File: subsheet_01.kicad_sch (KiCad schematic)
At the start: 0 parts

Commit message: schematic : place U1 and U2, the CPLD and the Gate array connector
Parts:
- added U1: ATF1508AS_L_100A_TQFP_JTAG_ENABLED_PHY, Package_QFP:TQFP-100_14x14mm_P0.5mm, symbol atf1508as-tqfp100-jtag:ATF1508AS_L_100A_TQFP_JTAG_ENABLED_PHY
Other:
- note added: "The north side of U1 is oriented toward the East side of U2, to hopefully have an easier routing of the 16 MHz clock."
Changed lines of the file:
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@@
     (comment 4 "Original repository : https://github.com/sporniket/...")
   )
+  (text "The north side of U1 is oriented toward the East side of U2,\nto hopefully have an easier routing of the 16 MHz clock."
+    (at 25.4 25.4 0)
+    (effects (font (size 2 2)) (justify left bottom))
+  )
+  (symbol (lib_id "atf1508as-tqfp100-jtag:ATF1508AS_L_100A_TQFP_JTAG_ENABLED_PHY") (at 106.68 130.81 270) (unit 1)
+    (in_bom yes) (on_board yes) (dnp no)
+    (property "Reference" "U1" (at 139.7 80.01 90)
+      (effects (font (size 1.27 1.27)) (justify left bottom))
+    )
+    (property "Value" "ATF1508AS_L_100A_TQFP_JTAG_ENABLED_PHY" (at 139.7 81.28 90)
+      (effects (font (size 1.27 1.27) bold) (justify left top))
+    )
+    (property "Footprint" "Package_QFP:TQFP-100_14x14mm_P0.5mm" (at 162.56 162.56 0)
+      (effects (font (size 1.27 1.27)) (justify left top) hide)
+    )
+    (property "Datasheet" "https://ww1.microchip.com/downloads/en/DeviceDoc/doc0784.pdf" (at 165.1 162.56 0)
+      (effects (font (size 1.27 1.27)) (justify left top) hide)
+    )
+    (pin "99")
+    (pin "45")
+    (pin "75")
+    (pin "74")
+    (pin "63")
+    (pin "81")
+    (pin "8")
+    (pin "35")
+    (pin "64")
+    (pin "72")
+    (pin "53")
+    (pin "38")
+    (pin "22")
+    (pin "69")
+    (pin "36")
+    (pin "71")
+    (pin "37")
+    (pin "88")
+    (pin "61")
+    (pin "82")
+    (pin "98")
+    (pin "96")
+    (pin "78")
+    (pin "34")
+    (pin "14")
+    (pin "1")
+    (pin "9")
+    (pin "49")
+    (pin "25")
+    (pin "84")
+    (pin "20")
+    (pin "41")
+    (pin "29")
+    (pin "4")
+    (pin "5")
+    (pin "42")
+    (pin "44")
+    (pin "46")
+    (pin "40")
+    (pin "43")
+    (pin "90")
+    (pin "28")
+    (pin "39")
+    (pin "2")
+    (pin "12")
+    (pin "13")
+    (pin "23")
+    (pin "24")
+    (pin "58")
+    (pin "11")
+    (pin "10")
+    (pin "100")
+    (pin "21")
+    (pin "68")
+    (pin "59")
+    (pin "52")
+    (pin "76")
+    (pin "15")
+    (pin "79")
+    (pin "86")
+    (pin "19")
+    (pin "66")
+    (pin "83")
+    (pin "7")
+    (pin "62")
+    (pin "89")
+    (pin "85")
+    (pin "16")
+    (pin "80")
+    (pin "51")
+    (pin "56")
+    (pin "94")
+    (pin "50")
+    (pin "77")
+    (pin "27")
+    (pin "26")
+    (pin "32")
+    (pin "93")
+    (pin "67")
+    (pin "54")
+    (pin "33")
+    (pin "97")
+    (pin "95")
+    (pin "30")
+    (pin "18")
+    (pin "3")
+    (pin "55")
+    (pin "91")
+    (pin "47")
+    (pin "70")
+    (pin "31")
+    (pin "87")
+    (pin "65")
+    (pin "6")
+    (pin "73")
+    (pin "17")
+    (pin "48")
+    (pin "57")
+    (pin "60")
+    (pin "92")
+    (instances
+      (project "mo5-ga-motorola-repl--atf1508"
+        (path "/04881907-557f-4bbf-81fb-63c3424a1f56/01c5ed34-7d13-4e1e-8741-0da82dc21da9"
+          (reference "U1") (unit 1)
+        )
+      )
+    )
+  )
 )

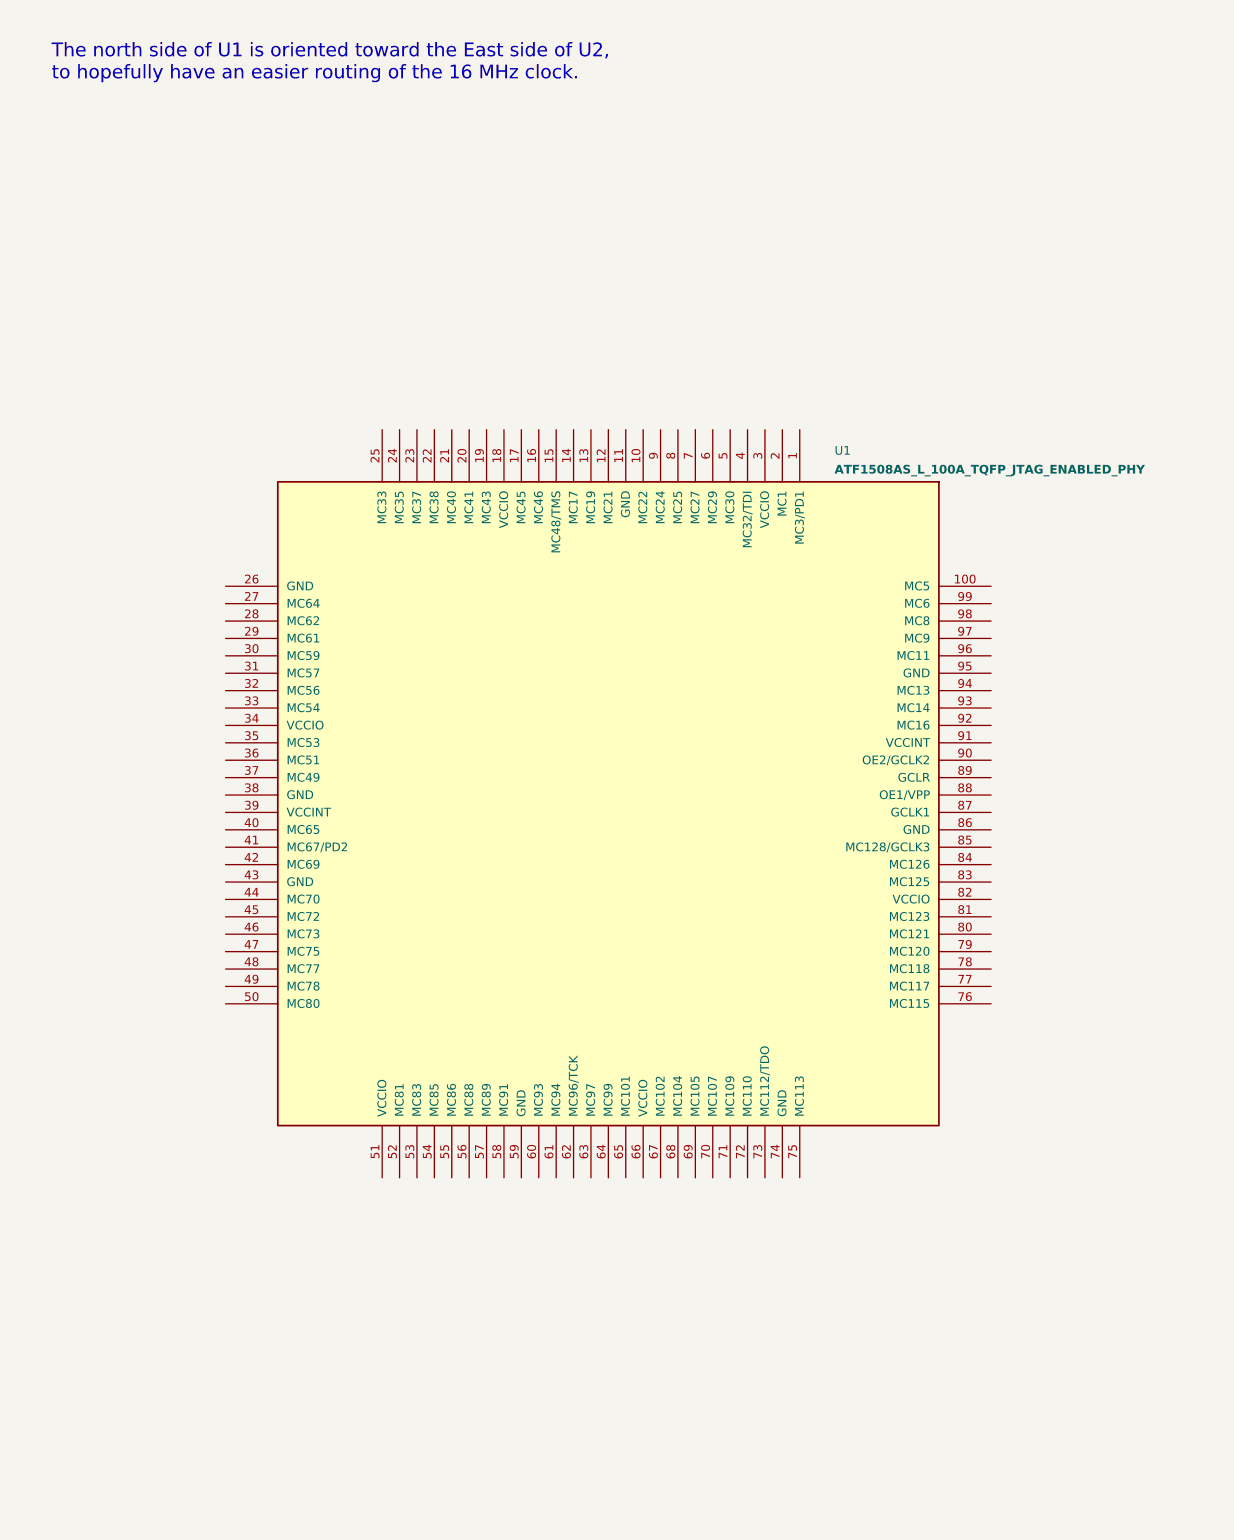
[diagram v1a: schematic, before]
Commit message: schematic : done U1, decoupling capacitors, pull resistors, JTAG and VPP connectors
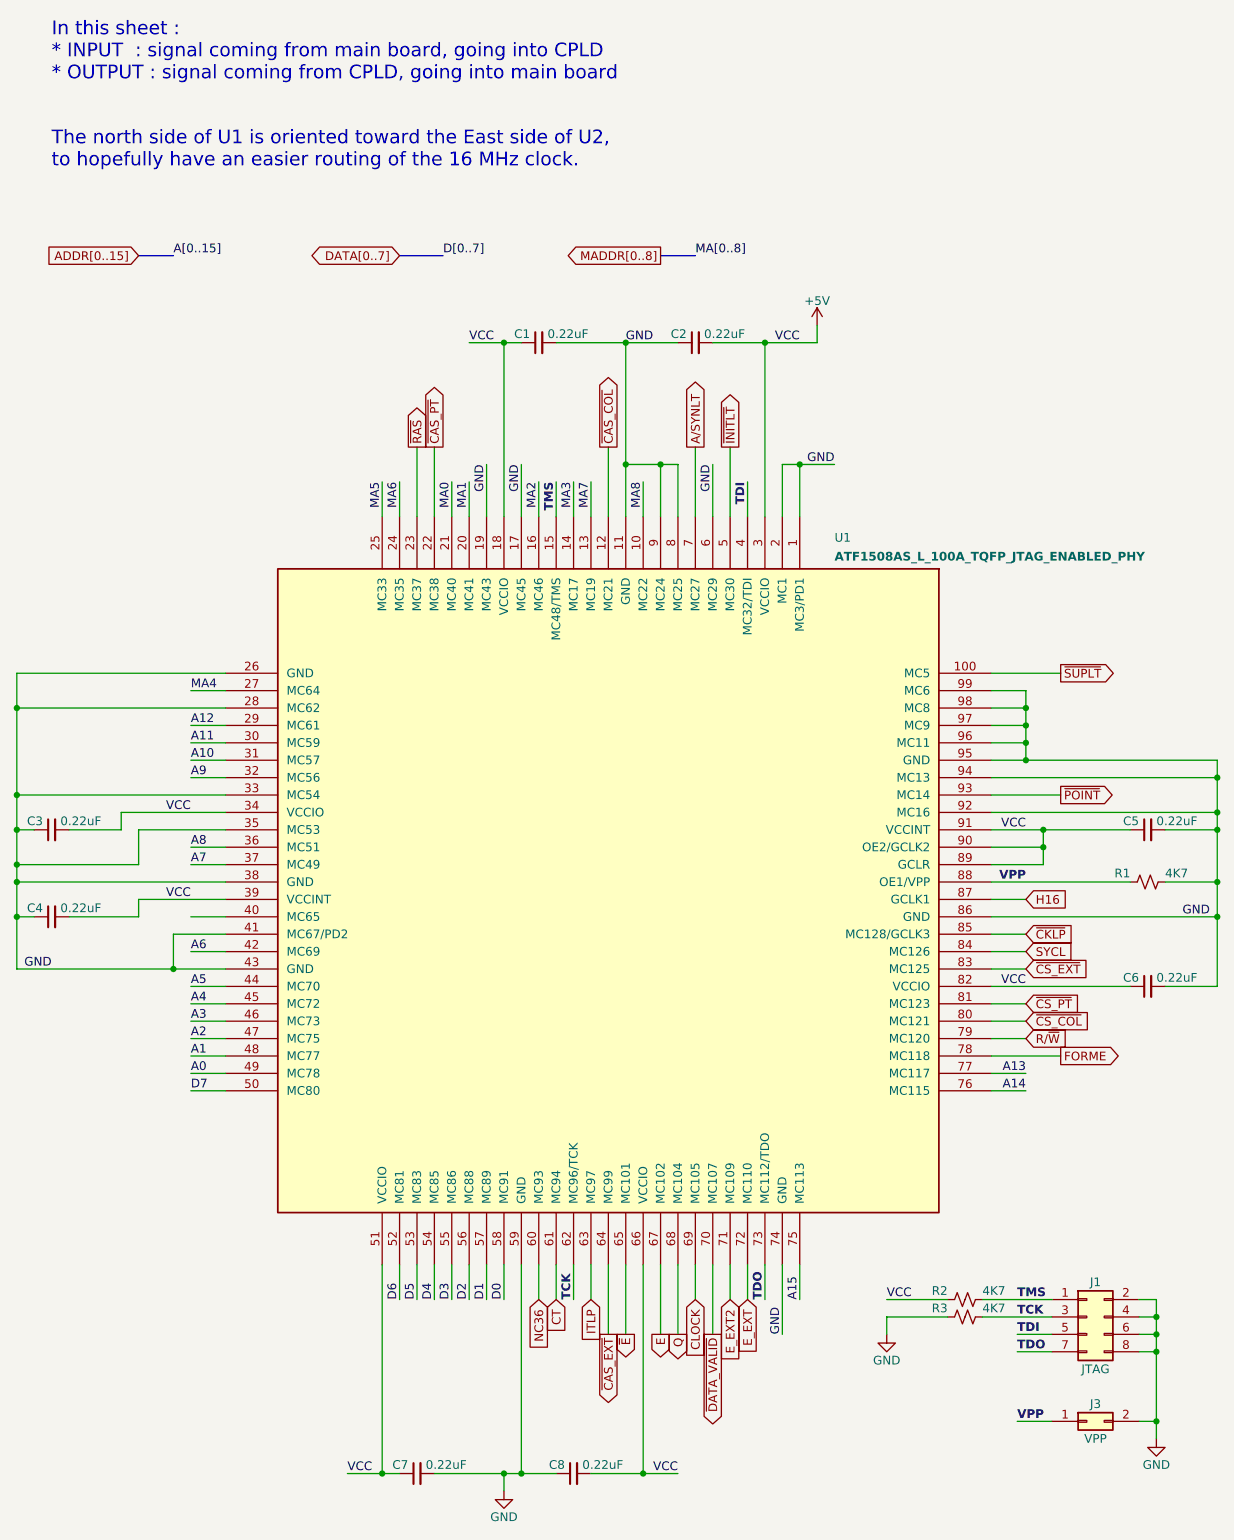
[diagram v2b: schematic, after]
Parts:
- added C1, C2, C3, C4, C5, C6, C7, C8: 0.22uF, symbol Device:C_Small
- added J1: JTAG, symbol Connector_Generic:Conn_02x04_Odd_Even
- added J3: VPP, symbol Connector_Generic:Conn_02x01
- added R1, R2, R3: 4K7, symbol Device:R_Small_US
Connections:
- net GND: now reaches U1.1 (MC3/PD1)
- net GND: now also U1.11 (GND), U1.17 (MC45), U1.19 (MC43), U1.2 (MC1), U1.26 (GND), U1.28 (MC62), U1.33 (MC54), U1.35 (MC53), U1.38 (GND), U1.41 (MC67/PD2), U1.43 (GND), U1.59 (GND), U1.6 (MC29), U1.74 (GND), U1.8 (MC25), U1.86 (GND), U1.9 (MC24), U1.92 (MC16), U1.94 (MC13), U1.95 (GND), U1.96 (MC11), U1.97 (MC9), U1.98 (MC8), U1.99 (MC6), C1.2, C2.1, C3.1, C4.1, C5.2, C6.2, C7.2, C8.1, J1.2 (Pin_2), J1.4 (Pin_4), J1.6 (Pin_6), J1.8 (Pin_8), J3.2 (Pin_2), R1.2, R3.1
- net MA8: now reaches U1.10 (MC22)
- net ~{SUPLT}: now reaches U1.100 (MC5)
- net ~{CAS_COL}: now reaches U1.12 (MC21)
- net MA7: now reaches U1.13 (MC19)
- net MA3: now reaches U1.14 (MC17)
- net TMS: now reaches U1.15 (MC48/TMS)
- net TMS: now also J1.1 (Pin_1), R2.2
- net MA2: now reaches U1.16 (MC46)
- net +5V: now reaches U1.18 (VCCIO)
- net +5V: now also U1.3 (VCCIO), U1.34 (VCCIO), U1.39 (VCCINT), U1.51 (VCCIO), U1.66 (VCCIO), U1.82 (VCCIO), U1.89 (GCLR), U1.90 (OE2/GCLK2), U1.91 (VCCINT), C1.1, C2.2, C3.2, C4.2, C5.1, C6.1, C7.1, C8.2, R2.1
- net MA1: now reaches U1.20 (MC41)
- net MA0: now reaches U1.21 (MC40)
- net ~{CAS_PT}: now reaches U1.22 (MC38)
- net ~{RAS}: now reaches U1.23 (MC37)
- net MA6: now reaches U1.24 (MC35)
- net MA5: now reaches U1.25 (MC33)
- net MA4: now reaches U1.27 (MC64)
- net A12: now reaches U1.29 (MC61)
- net A11: now reaches U1.30 (MC59)
- net A10: now reaches U1.31 (MC57)
- net A9: now reaches U1.32 (MC56)
- net A8: now reaches U1.36 (MC51)
- net A7: now reaches U1.37 (MC49)
- net TDI: now reaches U1.4 (MC32/TDI)
- net TDI: now also J1.5 (Pin_5)
- net A6: now reaches U1.42 (MC69)
- net A5: now reaches U1.44 (MC70)
- net A4: now reaches U1.45 (MC72)
- net A3: now reaches U1.46 (MC73)
- net A2: now reaches U1.47 (MC75)
- net A1: now reaches U1.48 (MC77)
- net A0: now reaches U1.49 (MC78)
- net ~{INITLT}: now reaches U1.5 (MC30)
- net D7: now reaches U1.50 (MC80)
- net D6: now reaches U1.52 (MC81)
- net D5: now reaches U1.53 (MC83)
- net D4: now reaches U1.54 (MC85)
- net D3: now reaches U1.55 (MC86)
- net D2: now reaches U1.56 (MC88)
- net D1: now reaches U1.57 (MC89)
- net D0: now reaches U1.58 (MC91)
- net NC36: now reaches U1.60 (MC93)
- net CT: now reaches U1.61 (MC94)
- net TCK: now reaches U1.62 (MC96/TCK)
- net TCK: now also J1.3 (Pin_3), R3.2
- net ITLP: now reaches U1.63 (MC97)
- net ~{CAS_EXT}: now reaches U1.64 (MC99)
- net ~{E}: now reaches U1.65 (MC101)
- net E: now reaches U1.67 (MC102)
- net Q: now reaches U1.68 (MC104)
- net CLOCK: now reaches U1.69 (MC105)
- net A/SYNLT: now reaches U1.7 (MC27)
- net ~{DATA_VALID}: now reaches U1.70 (MC107)
- net E_EXT2: now reaches U1.71 (MC109)
- net E_EXT: now reaches U1.72 (MC110)
- net TDO: now reaches U1.73 (MC112/TDO)
- net TDO: now also J1.7 (Pin_7)
- net A15: now reaches U1.75 (MC113)
- net A14: now reaches U1.76 (MC115)
- net A13: now reaches U1.77 (MC117)
- net FORME: now reaches U1.78 (MC118)
- net R/~{W}: now reaches U1.79 (MC120)
- net ~{CS_COL}: now reaches U1.80 (MC121)
- net ~{CS_PT}: now reaches U1.81 (MC123)
- net ~{CS_EXT}: now reaches U1.83 (MC125)
- net SYCL: now reaches U1.84 (MC126)
- net ~{CKLP}: now reaches U1.85 (MC128/GCLK3)
- net H16: now reaches U1.87 (GCLK1)
- net VPP: now reaches U1.88 (OE1/VPP)
- net VPP: now also J3.1 (Pin_1), R1.1
- net ~{POINT}: now reaches U1.93 (MC14)
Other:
- note added: "In this sheet : * INPUT : signal coming from main board, going into CPLD * OUTPUT : signal coming from CPLD, going into main board"
- moved on the sheet: U1

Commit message: pcb : draft
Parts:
- C1, C2, C3, C4, C5, C6, C7, C8: footprint (none) -> Capacitor_SMD:C_0603_1608Metric_Pad1.08x0.95mm_HandSolder
- J1: footprint (none) -> SpecialConnectors:PinHeader_2x04_P2.54mm_Vertical
- J3: footprint (none) -> SpecialConnectors:PinHeader_2x01_P2.54mm_Vertical
- R1, R2, R3: footprint (none) -> Resistor_SMD:R_0603_1608Metric_Pad0.98x0.95mm_HandSolder
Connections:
- net GND: now also U1.40 (MC65)
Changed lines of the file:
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@@
   (junction (at 20.32 116.84) (diameter 0) (color 0 0 0 0)
   )
+  (junction (at 43.18 149.86) (diameter 0) (color 0 0 0 0)
+  )
   (junction (at 129.54 63.5) (diameter 0) (color 0 0 0 0)
   )
@@
     (stroke (width 0) (type default))
   )
+  (wire (pts (xy 43.18 149.86) (xy 43.18 154.94))
+    (stroke (width 0) (type default))
+  )
   (wire (pts (xy 167.64 116.84) (xy 167.64 119.38))
     (stroke (width 0) (type default))
@@
     (stroke (width 0) (type default))
   )
-  (wire (pts (xy 43.18 149.86) (xy 43.18 154.94))
+  (wire (pts (xy 43.18 147.32) (xy 43.18 149.86))
     (stroke (width 0) (type default))
   )
@@
     (stroke (width 0) (type default))
   )
-  (wire (pts (xy 45.72 147.32) (xy 50.8 147.32))
+  (wire (pts (xy 43.18 147.32) (xy 50.8 147.32))
     (stroke (width 0) (type default))
   )
@@
       (effects (font (size 1.27 1.27)))
     )
-    (property "Footprint" "" (at 176.53 205.74 0)
+    (property "Footprint" "SpecialConnectors:PinHeader_2x04_P2.54mm_Vertical" (at 176.53 205.74 0)
       (effects (font (size 1.27 1.27)) hide)
     )
@@
       (effects (font (size 1.27 1.27)) (justify right))
     )
-    (property "Footprint" "" (at 185.42 142.24 0)
+    (property "Footprint" "Resistor_SMD:R_0603_1608Metric_Pad0.98x0.95mm_HandSolder" (at 185.42 142.24 0)
       (effects (font (size 1.27 1.27)) hide)
     )
@@
       (effects (font (size 1.27 1.27)) (justify right))
     )
-    (property "Footprint" "" (at 119.38 63.5 0)
+    (property "Footprint" "Capacitor_SMD:C_0603_1608Metric_Pad1.08x0.95mm_HandSolder" (at 119.38 63.5 0)
       (effects (font (size 1.27 1.27)) hide)
     )
@@
       (effects (font (size 1.27 1.27)) (justify right))
     )
-    (property "Footprint" "" (at 25.4 134.62 0)
+    (property "Footprint" "Capacitor_SMD:C_0603_1608Metric_Pad1.08x0.95mm_HandSolder" (at 25.4 134.62 0)
       (effects (font (size 1.27 1.27)) hide)
     )
@@
       (effects (font (size 1.27 1.27)) (justify right))
     )
-    (property "Footprint" "" (at 78.74 228.6 0)
+    (property "Footprint" "Capacitor_SMD:C_0603_1608Metric_Pad1.08x0.95mm_HandSolder" (at 78.74 228.6 0)
       (effects (font (size 1.27 1.27)) hide)
     )
@@
       (effects (font (size 1.27 1.27)) (justify right))
     )
-    (property "Footprint" "" (at 158.75 203.2 0)
+    (property "Footprint" "Resistor_SMD:R_0603_1608Metric_Pad0.98x0.95mm_HandSolder" (at 158.75 203.2 0)
       (effects (font (size 1.27 1.27)) hide)
     )
@@
       (effects (font (size 1.27 1.27)) (justify right))
     )
-    (property "Footprint" "" (at 185.42 134.62 0)
+    (property "Footprint" "Capacitor_SMD:C_0603_1608Metric_Pad1.08x0.95mm_HandSolder" (at 185.42 134.62 0)
       (effects (font (size 1.27 1.27)) hide)
     )
@@
       (effects (font (size 1.27 1.27)) (justify right))
     )
-    (property "Footprint" "" (at 185.42 157.48 0)
+    (property "Footprint" "Capacitor_SMD:C_0603_1608Metric_Pad1.08x0.95mm_HandSolder" (at 185.42 157.48 0)
       (effects (font (size 1.27 1.27)) hide)
     )
@@
       (effects (font (size 1.27 1.27)) (justify right))
     )
-    (property "Footprint" "" (at 158.75 205.74 0)
+    (property "Footprint" "Resistor_SMD:R_0603_1608Metric_Pad0.98x0.95mm_HandSolder" (at 158.75 205.74 0)
       (effects (font (size 1.27 1.27)) hide)
     )
@@
       (effects (font (size 1.27 1.27)) (justify right))
     )
-    (property "Footprint" "" (at 96.52 63.5 0)
+    (property "Footprint" "Capacitor_SMD:C_0603_1608Metric_Pad1.08x0.95mm_HandSolder" (at 96.52 63.5 0)
       (effects (font (size 1.27 1.27)) hide)
     )
@@
       (effects (font (size 1.27 1.27)) (justify right))
     )
-    (property "Footprint" "" (at 101.6 228.6 0)
+    (property "Footprint" "Capacitor_SMD:C_0603_1608Metric_Pad1.08x0.95mm_HandSolder" (at 101.6 228.6 0)
       (effects (font (size 1.27 1.27)) hide)
     )
@@
       (effects (font (size 1.27 1.27)))
     )
-    (property "Footprint" "" (at 176.53 220.98 0)
+    (property "Footprint" "SpecialConnectors:PinHeader_2x01_P2.54mm_Vertical" (at 176.53 220.98 0)
       (effects (font (size 1.27 1.27)) hide)
     )
@@
       (effects (font (size 1.27 1.27)) (justify right))
     )
-    (property "Footprint" "" (at 25.4 147.32 0)
-      (effects (font (size 1.27 1.27)) hide)
-    )
+    (property "Footprint" "Capacitor_SMD:C_0603_1608Metric_Pad1.08x0.95mm_HandSolder" (at 25.4 147.32 0)
+      (effects (font (size 1.27 1.27)) hide)
+    )
